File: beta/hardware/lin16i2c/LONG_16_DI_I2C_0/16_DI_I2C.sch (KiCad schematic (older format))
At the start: 105 parts, among them P1 CONN_2, P10 CONN_5, P12 CONN_5, P13 CONN_2, P2 CONN_2, P3 CONN_2, P4 CONN_2, P5 CONN_2, P6 CONN_2, P7 CONN_2, P8 CONN_2, U1 PCF8574, U2 PCF8574

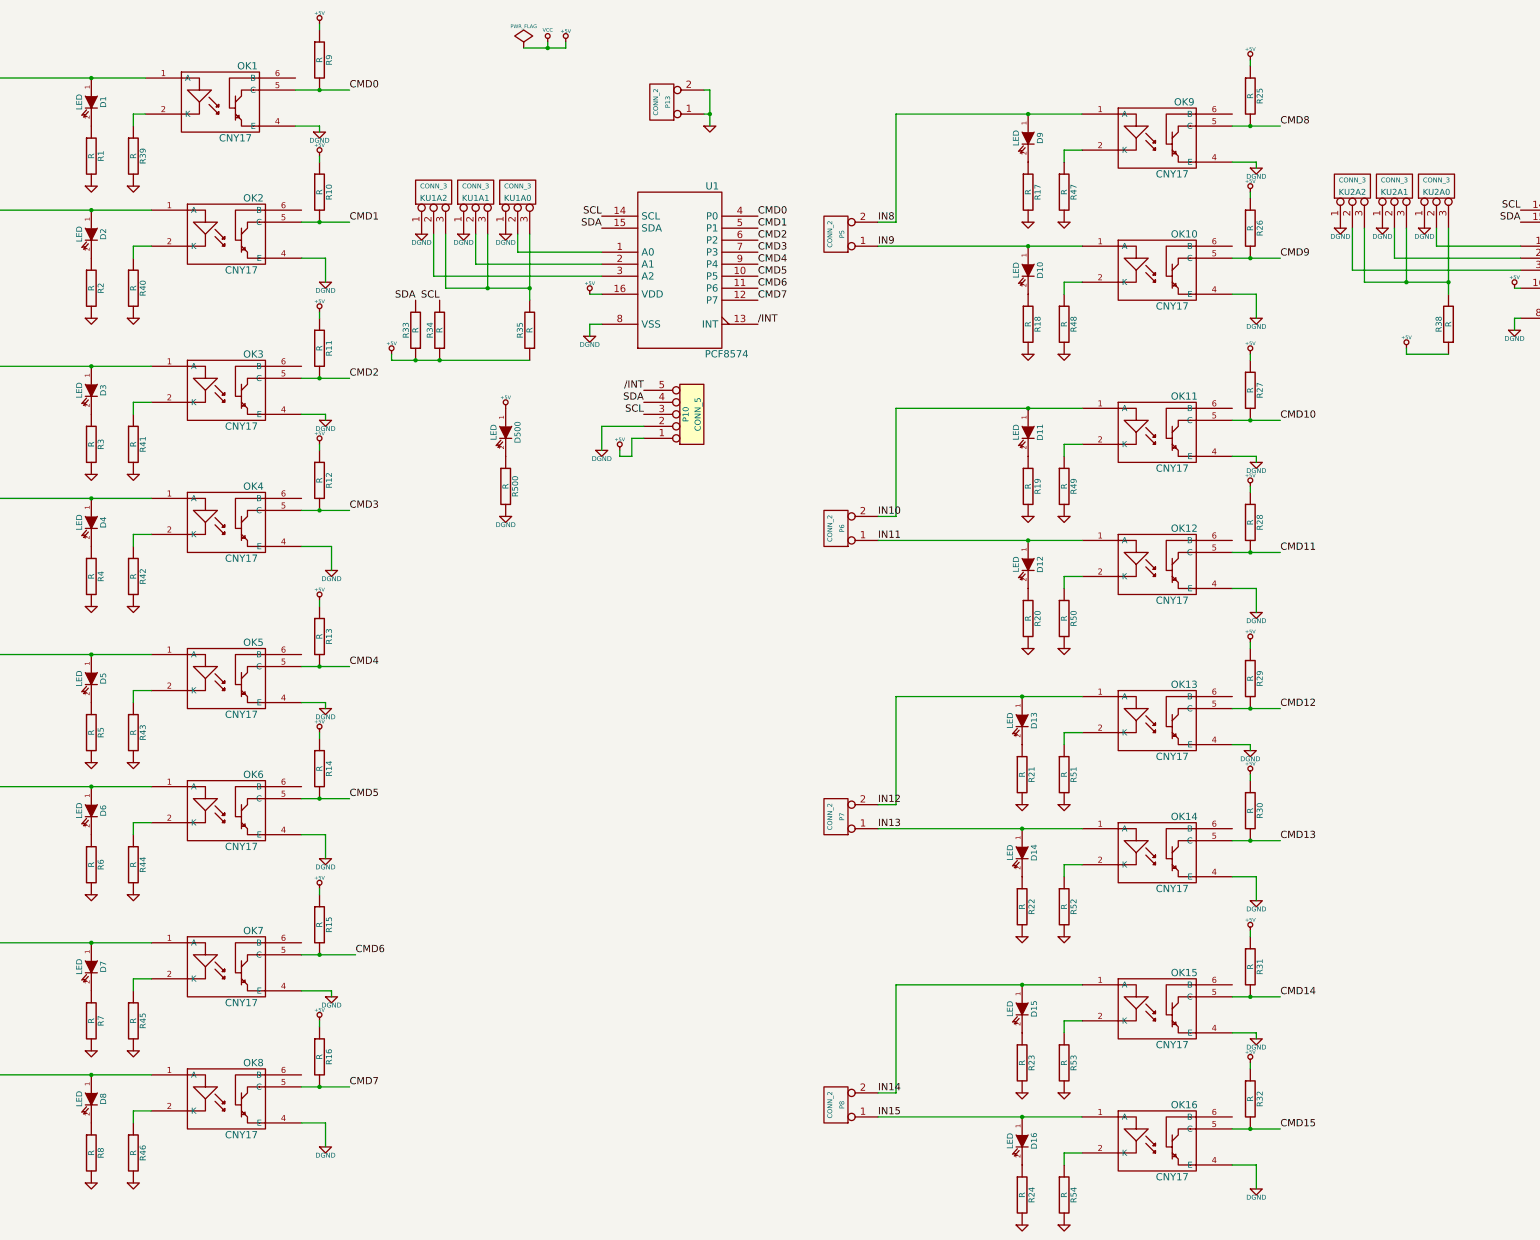
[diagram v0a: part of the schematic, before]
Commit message: ajout valeurs des resistances (? valider)
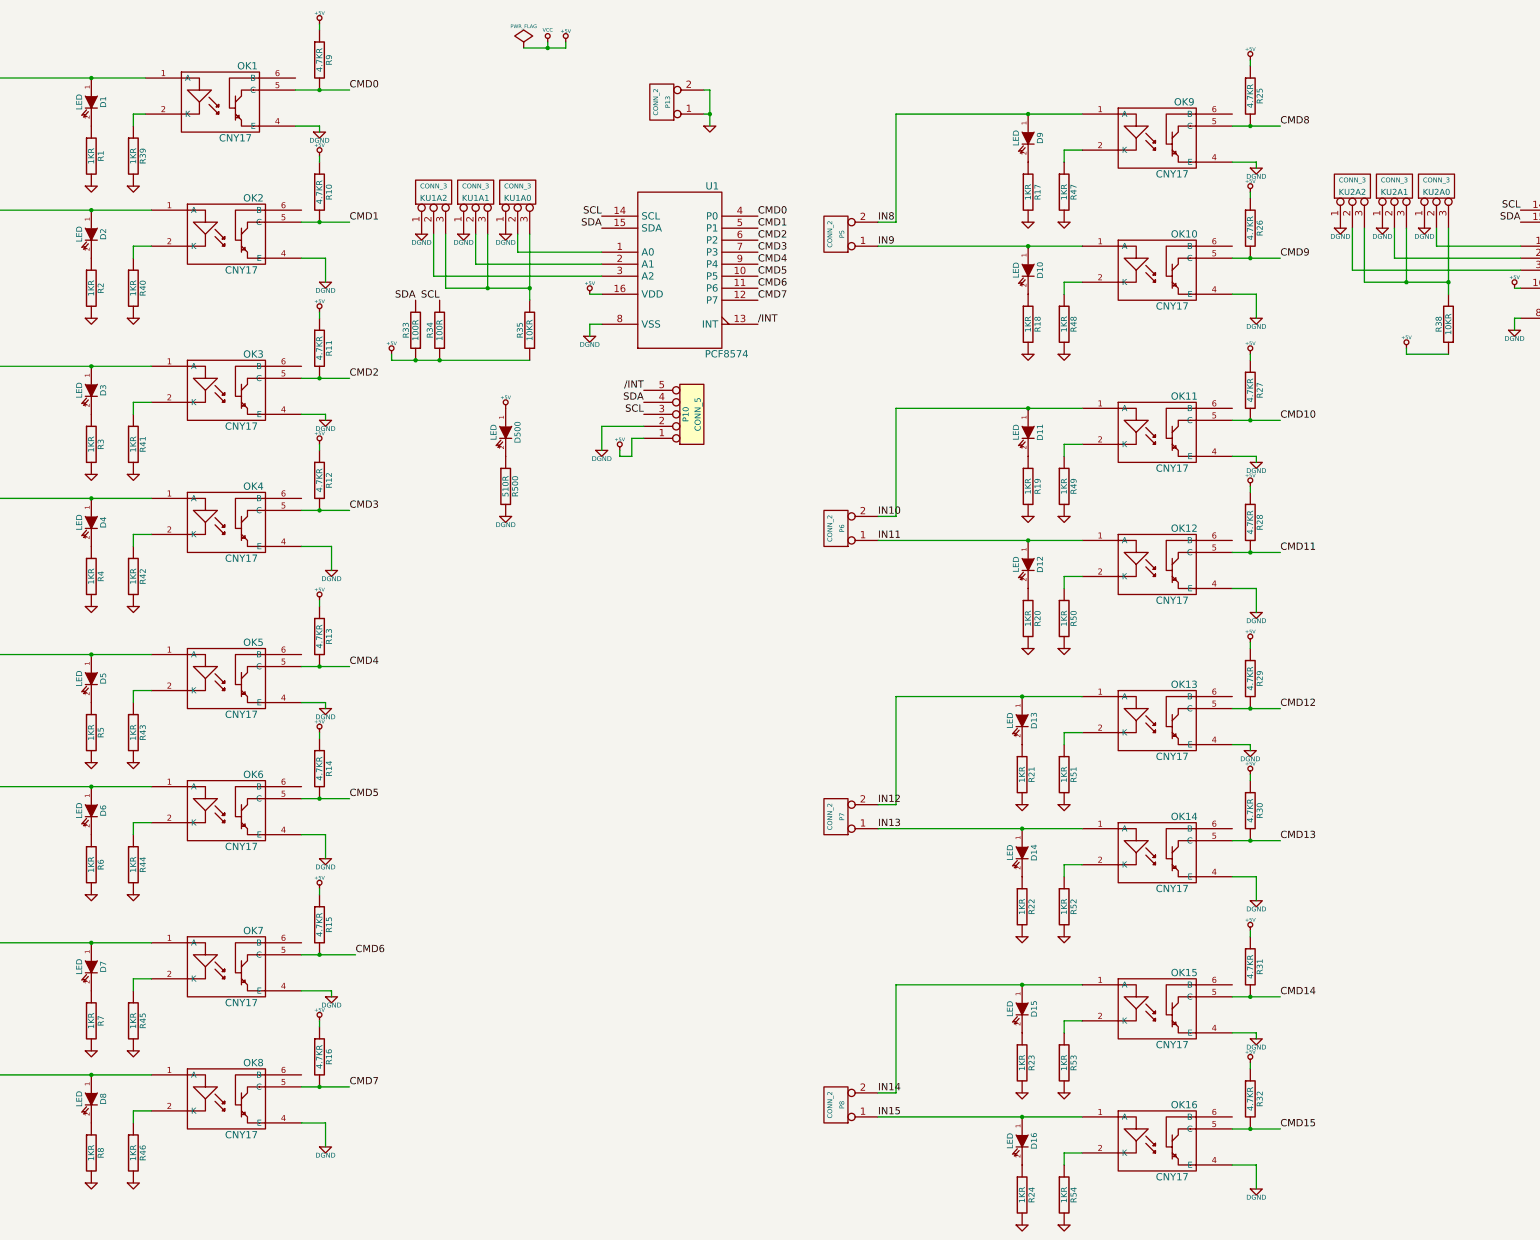
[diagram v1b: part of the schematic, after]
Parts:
- R1, R17, R18, R19, R2, R20, R21, R22, R23, R24, R3, R39, R4, R40, R41, R42, R43, R44, R45, R46, R47, R48, R49, R5, R50, R51, R52, R53, R54, R6, R7, R8: value R -> 1KR
- R10, R11, R12, R13, R14, R15, R16, R25, R26, R27, R28, R29, R30, R31, R32, R9: value R -> 4.7KR
- R33, R34: value R -> 100R
- R35, R38: value R -> 10KR
- R500: value R -> 510R
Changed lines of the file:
@@
-EESchema Schematic File Version 2  date mer. 02 mai 2012 10:46:34 CEST
+EESchema Schematic File Version 2  date ven. 18 mai 2012 22:19:33 CEST
 LIBS:power
 LIBS:device
@@
 Sheet 1 1
 Title "16 Digital Inputs Multiplexied Board"
-Date "2 may 2012"
+Date "18 may 2012"
 Rev "draft"
 Comp "XPLDUINO project"
@@
 P 5900 4500
 F 0 "R500" V 5980 4500 50  0000 C CNN
-F 1 "R" V 5900 4500 50  0000 C CNN
+F 1 "510R" V 5900 4500 50  0000 C CNN
 	1    5900 4500
 	1    0    0    -1
@@
 P 10550 10400
 F 0 "R54" V 10630 10400 50  0000 C CNN
-F 1 "R" V 10550 10400 50  0000 C CNN
+F 1 "1KR" V 10550 10400 50  0000 C CNN
 	1    10550 10400
 	1    0    0    -1
@@
 P 10550 9300
 F 0 "R53" V 10630 9300 50  0000 C CNN
-F 1 "R" V 10550 9300 50  0000 C CNN
+F 1 "1KR" V 10550 9300 50  0000 C CNN
 	1    10550 9300
 	1    0    0    -1
@@
 P 10550 8000
 F 0 "R52" V 10630 8000 50  0000 C CNN
-F 1 "R" V 10550 8000 50  0000 C CNN
+F 1 "1KR" V 10550 8000 50  0000 C CNN
 	1    10550 8000
 	1    0    0    -1
@@
 P 10550 6900
 F 0 "R51" V 10630 6900 50  0000 C CNN
-F 1 "R" V 10550 6900 50  0000 C CNN
+F 1 "1KR" V 10550 6900 50  0000 C CNN
 	1    10550 6900
 	1    0    0    -1
@@
 P 10550 5600
 F 0 "R50" V 10630 5600 50  0000 C CNN
-F 1 "R" V 10550 5600 50  0000 C CNN
+F 1 "1KR" V 10550 5600 50  0000 C CNN
 	1    10550 5600
 	1    0    0    -1
@@
 P 10550 4500
 F 0 "R49" V 10630 4500 50  0000 C CNN
-F 1 "R" V 10550 4500 50  0000 C CNN
+F 1 "1KR" V 10550 4500 50  0000 C CNN
 	1    10550 4500
 	1    0    0    -1
@@
 P 10550 3150
 F 0 "R48" V 10630 3150 50  0000 C CNN
-F 1 "R" V 10550 3150 50  0000 C CNN
+F 1 "1KR" V 10550 3150 50  0000 C CNN
 	1    10550 3150
 	1    0    0    -1
@@
 P 10550 2050
 F 0 "R47" V 10630 2050 50  0000 C CNN
-F 1 "R" V 10550 2050 50  0000 C CNN
+F 1 "1KR" V 10550 2050 50  0000 C CNN
 	1    10550 2050
 	1    0    0    -1
@@
 P 2800 10050
 F 0 "R46" V 2880 10050 50  0000 C CNN
-F 1 "R" V 2800 10050 50  0000 C CNN
+F 1 "1KR" V 2800 10050 50  0000 C CNN
 	1    2800 10050
 	1    0    0    -1
@@
 P 2800 8950
 F 0 "R45" V 2880 8950 50  0000 C CNN
-F 1 "R" V 2800 8950 50  0000 C CNN
+F 1 "1KR" V 2800 8950 50  0000 C CNN
 	1    2800 8950
 	1    0    0    -1
@@
 P 2800 7650
 F 0 "R44" V 2880 7650 50  0000 C CNN
-F 1 "R" V 2800 7650 50  0000 C CNN
+F 1 "1KR" V 2800 7650 50  0000 C CNN
 	1    2800 7650
 	1    0    0    -1
@@
 P 2800 6550
 F 0 "R43" V 2880 6550 50  0000 C CNN
-F 1 "R" V 2800 6550 50  0000 C CNN
+F 1 "1KR" V 2800 6550 50  0000 C CNN
 	1    2800 6550
 	1    0    0    -1
@@
 P 2800 5250
 F 0 "R42" V 2880 5250 50  0000 C CNN
-F 1 "R" V 2800 5250 50  0000 C CNN
+F 1 "1KR" V 2800 5250 50  0000 C CNN
 	1    2800 5250
 	1    0    0    -1
@@
 P 2800 4150
 F 0 "R41" V 2880 4150 50  0000 C CNN
-F 1 "R" V 2800 4150 50  0000 C CNN
+F 1 "1KR" V 2800 4150 50  0000 C CNN
 	1    2800 4150
 	1    0    0    -1
@@
 P 2800 2850
 F 0 "R40" V 2880 2850 50  0000 C CNN
-F 1 "R" V 2800 2850 50  0000 C CNN
+F 1 "1KR" V 2800 2850 50  0000 C CNN
 	1    2800 2850
 	1    0    0    -1
@@
 P 2800 1750
 F 0 "R39" V 2880 1750 50  0000 C CNN
-F 1 "R" V 2800 1750 50  0000 C CNN
+F 1 "1KR" V 2800 1750 50  0000 C CNN
 	1    2800 1750
 	1    0    0    -1
@@
 P 13750 3150
 F 0 "R38" V 13830 3150 50  0000 C CNN
-F 1 "R" V 13750 3150 50  0000 C CNN
+F 1 "10KR" V 13750 3150 50  0000 C CNN
 	1    13750 3150
 	-1   0    0    1
@@
 P 5150 3200
 F 0 "R33" V 5230 3200 50  0000 C CNN
-F 1 "R" V 5150 3200 50  0000 C CNN
+F 1 "100R" V 5150 3200 50  0000 C CNN
 	1    5150 3200
 	-1   0    0    1
@@
 P 6100 3200
 F 0 "R35" V 6180 3200 50  0000 C CNN
-F 1 "R" V 6100 3200 50  0000 C CNN
+F 1 "10KR" V 6100 3200 50  0000 C CNN
 	1    6100 3200
 	-1   0    0    1
@@
 P 5350 3200
 F 0 "R34" V 5430 3200 50  0000 C CNN
-F 1 "R" V 5350 3200 50  0000 C CNN
+F 1 "100R" V 5350 3200 50  0000 C CNN
 	1    5350 3200
 	-1   0    0    1
@@
 P 10250 2050
 F 0 "R17" V 10330 2050 50  0000 C CNN
-F 1 "R" V 10250 2050 50  0000 C CNN
+F 1 "1KR" V 10250 2050 50  0000 C CNN
 	1    10250 2050
 	1    0    0    -1
@@
 P 12100 1250
 F 0 "R25" V 12180 1250 50  0000 C CNN
-F 1 "R" V 12100 1250 50  0000 C CNN
+F 1 "4.7KR" V 12100 1250 50  0000 C CNN
 	1    12100 1250
 	1    0    0    -1
@@
 P 12100 2350
 F 0 "R26" V 12180 2350 50  0000 C CNN
-F 1 "R" V 12100 2350 50  0000 C CNN
+F 1 "4.7KR" V 12100 2350 50  0000 C CNN
 	1    12100 2350
 	1    0    0    -1
@@
 P 10250 3150
 F 0 "R18" V 10330 3150 50  0000 C CNN
-F 1 "R" V 10250 3150 50  0000 C CNN
+F 1 "1KR" V 10250 3150 50  0000 C CNN
 	1    10250 3150
 	1    0    0    -1
@@
 P 10250 5600
 F 0 "R20" V 10330 5600 50  0000 C CNN
-F 1 "R" V 10250 5600 50  0000 C CNN
+F 1 "1KR" V 10250 5600 50  0000 C CNN
 	1    10250 5600
 	1    0    0    -1
@@
 P 12100 4800
 F 0 "R28" V 12180 4800 50  0000 C CNN
-F 1 "R" V 12100 4800 50  0000 C CNN
+F 1 "4.7KR" V 12100 4800 50  0000 C CNN
 	1    12100 4800
 	1    0    0    -1
@@
 P 12100 3700
 F 0 "R27" V 12180 3700 50  0000 C CNN
-F 1 "R" V 12100 3700 50  0000 C CNN
+F 1 "4.7KR" V 12100 3700 50  0000 C CNN
 	1    12100 3700
 	1    0    0    -1
@@
 P 10250 4500
 F 0 "R19" V 10330 4500 50  0000 C CNN
-F 1 "R" V 10250 4500 50  0000 C CNN
+F 1 "1KR" V 10250 4500 50  0000 C CNN
 	1    10250 4500
 	1    0    0    -1
@@
 P 10200 9300
 F 0 "R23" V 10280 9300 50  0000 C CNN
-F 1 "R" V 10200 9300 50  0000 C CNN
+F 1 "1KR" V 10200 9300 50  0000 C CNN
 	1    10200 9300
 	1    0    0    -1
@@
 P 12100 8500
 F 0 "R31" V 12180 8500 50  0000 C CNN
-F 1 "R" V 12100 8500 50  0000 C CNN
+F 1 "4.7KR" V 12100 8500 50  0000 C CNN
 	1    12100 8500
 	1    0    0    -1
@@
 P 12100 9600
 F 0 "R32" V 12180 9600 50  0000 C CNN
-F 1 "R" V 12100 9600 50  0000 C CNN
+F 1 "4.7KR" V 12100 9600 50  0000 C CNN
 	1    12100 9600
 	1    0    0    -1
@@
 P 10200 10400
 F 0 "R24" V 10280 10400 50  0000 C CNN
-F 1 "R" V 10200 10400 50  0000 C CNN
+F 1 "1KR" V 10200 10400 50  0000 C CNN
 	1    10200 10400
 	1    0    0    -1
@@
 P 10200 8000
 F 0 "R22" V 10280 8000 50  0000 C CNN
-F 1 "R" V 10200 8000 50  0000 C CNN
+F 1 "1KR" V 10200 8000 50  0000 C CNN
 	1    10200 8000
 	1    0    0    -1
@@
 P 12100 7200
 F 0 "R30" V 12180 7200 50  0000 C CNN
-F 1 "R" V 12100 7200 50  0000 C CNN
+F 1 "4.7KR" V 12100 7200 50  0000 C CNN
 	1    12100 7200
 	1    0    0    -1
@@
 P 12100 6100
 F 0 "R29" V 12180 6100 50  0000 C CNN
-F 1 "R" V 12100 6100 50  0000 C CNN
+F 1 "4.7KR" V 12100 6100 50  0000 C CNN
 	1    12100 6100
 	1    0    0    -1
@@
 P 10200 6900
 F 0 "R21" V 10280 6900 50  0000 C CNN
-F 1 "R" V 10200 6900 50  0000 C CNN
+F 1 "1KR" V 10200 6900 50  0000 C CNN
 	1    10200 6900
 	1    0    0    -1
@@
 P 2450 6550
 F 0 "R5" V 2530 6550 50  0000 C CNN
-F 1 "R" V 2450 6550 50  0000 C CNN
+F 1 "1KR" V 2450 6550 50  0000 C CNN
 	1    2450 6550
 	1    0    0    -1
@@
 P 4350 5750
 F 0 "R13" V 4430 5750 50  0000 C CNN
-F 1 "R" V 4350 5750 50  0000 C CNN
+F 1 "4.7KR" V 4350 5750 50  0000 C CNN
 	1    4350 5750
 	1    0    0    -1
@@
 P 4350 6850
 F 0 "R14" V 4430 6850 50  0000 C CNN
-F 1 "R" V 4350 6850 50  0000 C CNN
+F 1 "4.7KR" V 4350 6850 50  0000 C CNN
 	1    4350 6850
 	1    0    0    -1
@@
 P 2450 7650
 F 0 "R6" V 2530 7650 50  0000 C CNN
-F 1 "R" V 2450 7650 50  0000 C CNN
+F 1 "1KR" V 2450 7650 50  0000 C CNN
 	1    2450 7650
 	1    0    0    -1
@@
 P 2450 10050
 F 0 "R8" V 2530 10050 50  0000 C CNN
-F 1 "R" V 2450 10050 50  0000 C CNN
+F 1 "1KR" V 2450 10050 50  0000 C CNN
 	1    2450 10050
 	1    0    0    -1
@@
 P 4350 9250
 F 0 "R16" V 4430 9250 50  0000 C CNN
-F 1 "R" V 4350 9250 50  0000 C CNN
+F 1 "4.7KR" V 4350 9250 50  0000 C CNN
 	1    4350 9250
 	1    0    0    -1
@@
 P 4350 8150
 F 0 "R15" V 4430 8150 50  0000 C CNN
-F 1 "R" V 4350 8150 50  0000 C CNN
+F 1 "4.7KR" V 4350 8150 50  0000 C CNN
 	1    4350 8150
 	1    0    0    -1
@@
 P 2450 8950
 F 0 "R7" V 2530 8950 50  0000 C CNN
-F 1 "R" V 2450 8950 50  0000 C CNN
+F 1 "1KR" V 2450 8950 50  0000 C CNN
 	1    2450 8950
 	1    0    0    -1
@@
 P 2450 4150
 F 0 "R3" V 2530 4150 50  0000 C CNN
-F 1 "R" V 2450 4150 50  0000 C CNN
+F 1 "1KR" V 2450 4150 50  0000 C CNN
 	1    2450 4150
 	1    0    0    -1
@@
 P 4350 3350
 F 0 "R11" V 4430 3350 50  0000 C CNN
-F 1 "R" V 4350 3350 50  0000 C CNN
+F 1 "4.7KR" V 4350 3350 50  0000 C CNN
 	1    4350 3350
 	1    0    0    -1
@@
 P 4350 4450
 F 0 "R12" V 4430 4450 50  0000 C CNN
-F 1 "R" V 4350 4450 50  0000 C CNN
+F 1 "4.7KR" V 4350 4450 50  0000 C CNN
 	1    4350 4450
 	1    0    0    -1
@@
 P 2450 5250
 F 0 "R4" V 2530 5250 50  0000 C CNN
-F 1 "R" V 2450 5250 50  0000 C CNN
+F 1 "1KR" V 2450 5250 50  0000 C CNN
 	1    2450 5250
 	1    0    0    -1
@@
 P 2450 2850
 F 0 "R2" V 2530 2850 50  0000 C CNN
-F 1 "R" V 2450 2850 50  0000 C CNN
+F 1 "1KR" V 2450 2850 50  0000 C CNN
 	1    2450 2850
 	1    0    0    -1
@@
 P 4350 2050
 F 0 "R10" V 4430 2050 50  0000 C CNN
-F 1 "R" V 4350 2050 50  0000 C CNN
+F 1 "4.7KR" V 4350 2050 50  0000 C CNN
 	1    4350 2050
 	1    0    0    -1
@@
 P 4350 950
 F 0 "R9" V 4430 950 50  0000 C CNN
-F 1 "R" V 4350 950 50  0000 C CNN
+F 1 "4.7KR" V 4350 950 50  0000 C CNN
 	1    4350 950
 	1    0    0    -1
@@
 P 2450 1750
 F 0 "R1" V 2530 1750 50  0000 C CNN
-F 1 "R" V 2450 1750 50  0000 C CNN
+F 1 "1KR" V 2450 1750 50  0000 C CNN
 	1    2450 1750
 	1    0    0    -1
